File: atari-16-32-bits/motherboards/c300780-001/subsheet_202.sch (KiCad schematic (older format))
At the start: 15 parts, among them J203 DB25 Parallel port

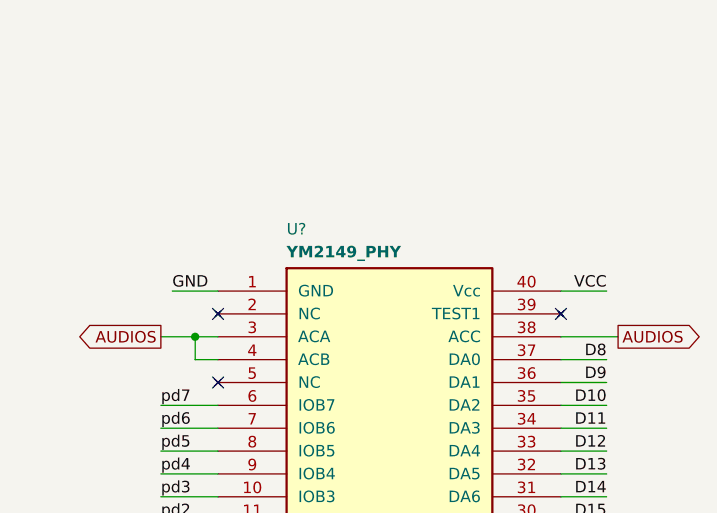
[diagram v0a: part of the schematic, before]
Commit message: subsheet 303 : sclk and clk2
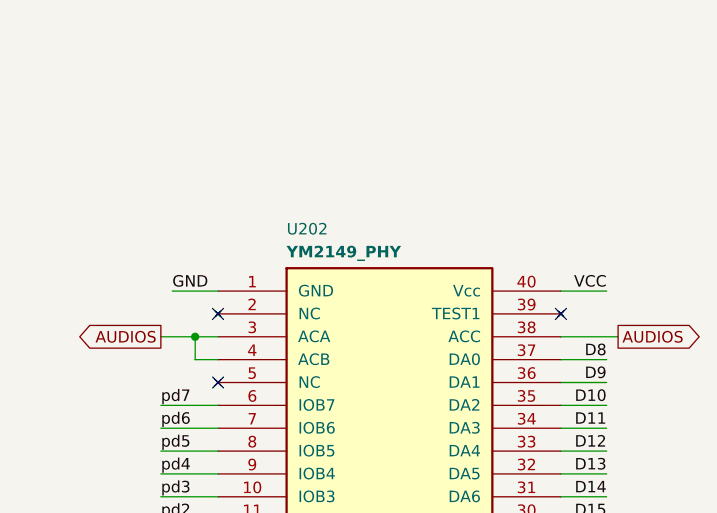
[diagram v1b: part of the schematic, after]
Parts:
- gave numbers to parts that had none: 1
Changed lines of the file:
@@
 $Descr A4 8268 11693 portrait
 encoding utf-8
-Sheet 11 17
+Sheet 11 18
 Title ""
 Date ""
@@
 AUDIOS
 $Comp
-L ym2149:YM2149_PHY U?
+L ym2149:YM2149_PHY U202
 U 1 1 608ED38D
 P 2450 3050
-F 0 "U?" H 2000 4300 50  0000 L TNN
+F 0 "U202" H 2000 4300 50  0000 L TNN
 F 1 "YM2149_PHY" H 2000 4200 50  0000 L TNB
 F 2 "Package_DIP:DIP-40_W15.24mm_LongPads" H 2000 4400 50  0001 L TNN
